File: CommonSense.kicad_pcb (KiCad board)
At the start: 2 copper layers, 35 x 24 mm, 36 parts, among them J1 Conn_02x04_Counter_Clockwise, J2 Conn_01x02, J3 Conn_01x02, J5 Conn_ARM_SWD_TagConnect_TC203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, U1 NRF52810-QFAA-R7, U2 SHT41-AD1B-R2, Y1 ECS-.327-12.5-12R-TR, Y2 ABM11W-32.0000MHZ-7-D1X-T3

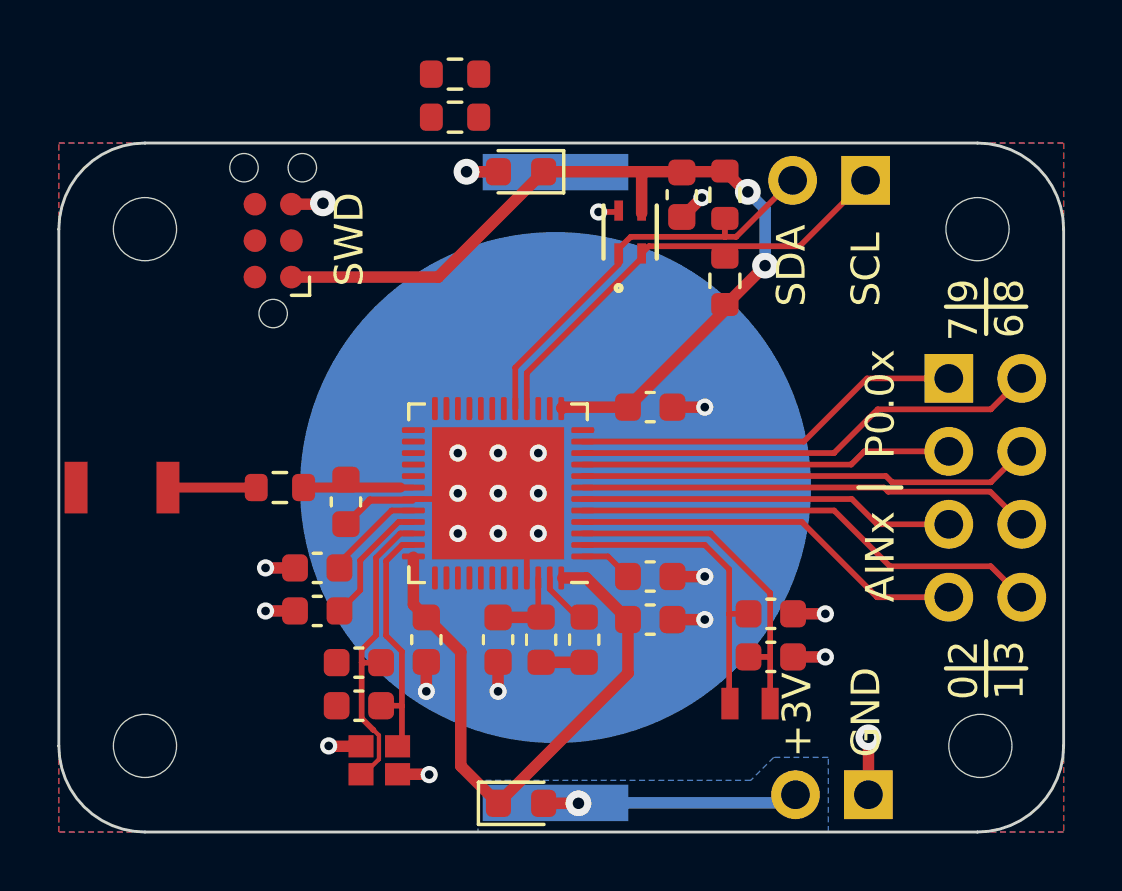
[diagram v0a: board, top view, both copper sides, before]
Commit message: Re-route SWD connector
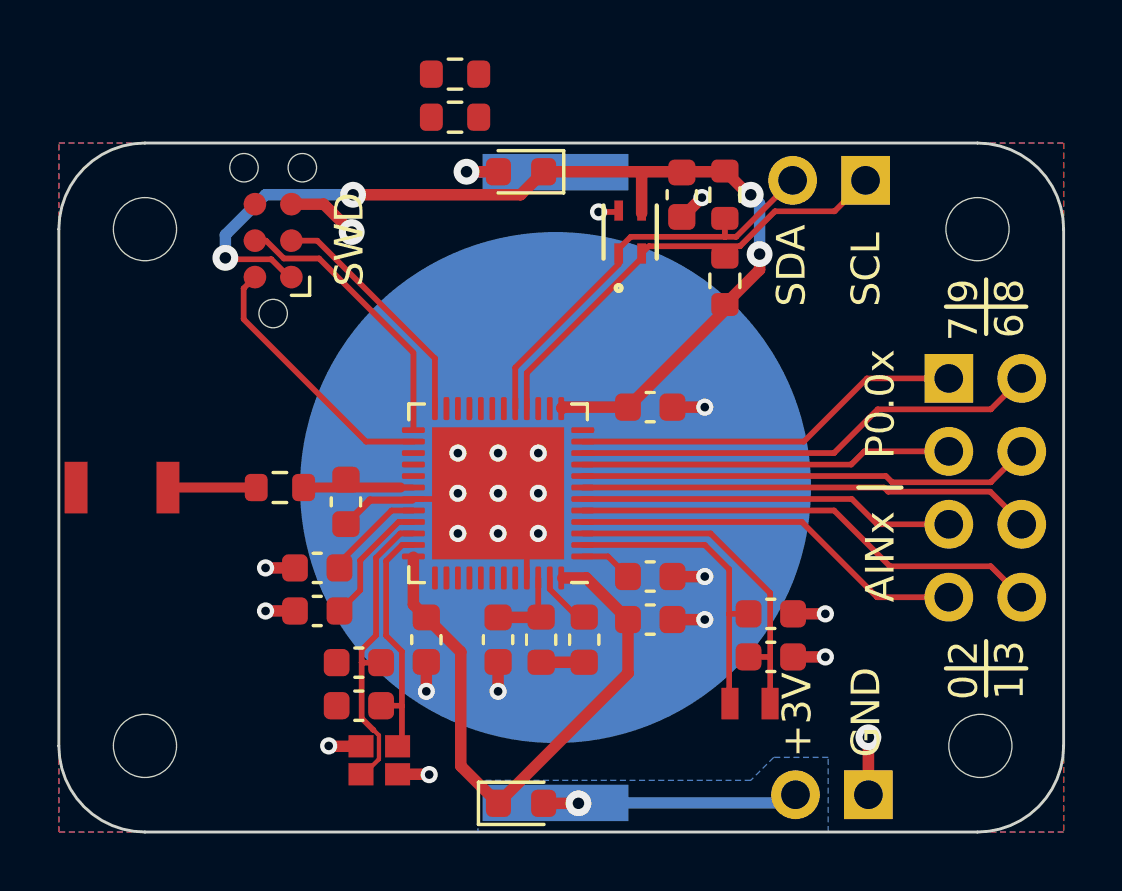
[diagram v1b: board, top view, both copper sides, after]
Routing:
- net /SWDCLK: track 0.00 -> 9.83 mm
- net /SWDIO: track 0.00 -> 9.31 mm
- net /NRESET: track 0.00 -> 8.45 mm
- net +3V0: track 52.2 -> 57.1 mm, vias 2 -> 4
- net GND: track 24.4 -> 25.8 mm
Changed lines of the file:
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@@
   )
   (segment (start 142.875 68) (end 139.8 68) (width 0.35) (layer "F.Cu") (net 1))
+  (segment (start 145.23 58.13) (end 144.1 58.13) (width 0.4) (layer "F.Cu") (net 2))
+  (segment (start 146.2 59.1) (end 145.23 58.13) (width 0.4) (layer "F.Cu") (net 2))
   (segment (start 148.887 77.987) (end 148.9 78) (width 0.4) (layer "F.Cu") (net 2))
   (segment (start 149.7 68.4) (end 149.9 68.2) (width 0.2) (layer "F.Cu") (net 2))
@@
   (segment (start 157.725 58.575) (end 158.4 57.9) (width 0.4) (layer "F.Cu") (net 2))
   (segment (start 145.413 77.013) (end 145.4 77) (width 0.4) (layer "F.Cu") (net 2))
-  (segment (start 144.1 58.13) (end 145.17 58.13) (width 0.4) (layer "F.Cu") (net 2))
   (segment (start 143.2 70.8) (end 144.225 70.8) (width 0.4) (layer "F.Cu") (net 2))
   (segment (start 157.7 58.575) (end 157.725 58.575) (width 0.4) (layer "F.Cu") (net 2))
@@
   (segment (start 161.575 72.4) (end 162.7 72.4) (width 0.4) (layer "F.Cu") (net 2))
   (segment (start 151.3 74.075) (end 151.3 75.1) (width 0.4) (layer "F.Cu") (net 2))
-  (segment (start 145.17 58.13) (end 145.2 58.1) (width 0.4) (layer "F.Cu") (net 2))
   (segment (start 154.8 58.4) (end 155.45305 58.4) (width 0.2) (layer "F.Cu") (net 2))
   (segment (start 146.5255 77.013) (end 145.413 77.013) (width 0.4) (layer "F.Cu") (net 2))
@@
   (via (at 151.3 69.6) (size 0.6) (drill 0.3) (layers "F.Cu" "B.Cu") (net 2))
   (via (at 158.5 71.1) (size 0.6) (drill 0.3) (layers "F.Cu" "B.Cu") (net 2))
-  (via (at 145.2 58.1) (size 0.9) (drill 0.4) (layers "F.Cu" "B.Cu") (net 2))
+  (via (at 146.2 59.1) (size 0.9) (drill 0.4) (layers "F.Cu" "B.Cu") (net 2))
   (via (at 148.9 78) (size 0.6) (drill 0.3) (layers "F.Cu" "B.Cu") (net 2))
   (via (at 149.9 68.2) (size 0.6) (drill 0.3) (layers "F.Cu" "B.Cu") (net 2))
@@
   (segment (start 154.25 69.2) (end 161.881891 69.2) (width 0.2) (layer "F.Cu") (net 21))
   (segment (start 161.881891 69.2) (end 164.501891 71.82) (width 0.2) (layer "F.Cu") (net 21))
+  (segment (start 143.8357 60.0207) (end 145.065991 60.0207) (width 0.2) (layer "F.Cu") (net 32))
+  (segment (start 143.215 59.4) (end 143.8357 60.0207) (width 0.2) (layer "F.Cu") (net 32))
+  (segment (start 148.35 63.304709) (end 148.35 66) (width 0.2) (layer "F.Cu") (net 32))
+  (segment (start 142.83 59.4) (end 143.215 59.4) (width 0.2) (layer "F.Cu") (net 32))
+  (segment (start 145.065991 60.0207) (end 148.35 63.304709) (width 0.2) (layer "F.Cu") (net 32))
+  (segment (start 142.83 60.67) (end 142.436301 61.063699) (width 0.2) (layer "F.Cu") (net 33))
+  (segment (start 142.436301 61.063699) (end 142.436301 62.136301) (width 0.2) (layer "F.Cu") (net 33))
+  (segment (start 142.436301 62.136301) (end 146.7 66.4) (width 0.2) (layer "F.Cu") (net 33))
+  (segment (start 146.7 66.4) (end 148.35 66.4) (width 0.2) (layer "F.Cu") (net 33))
   (segment (start 151.9 65.25) (end 151.9 63.822201) (width 0.2) (layer "F.Cu") (net 43))
   (segment (start 155.92025 59.266701) (end 159.2 59.266701) (width 0.2) (layer "F.Cu") (net 43))
@@
   (segment (start 151.9 63.822201) (end 155.49995 60.222251) (width 0.2) (layer "F.Cu") (net 43))
   (segment (start 155.49995 59.687001) (end 155.92025 59.266701) (width 0.2) (layer "F.Cu") (net 43))
-  (segment (start 156.553249 59.593701) (end 161.806299 59.593701) (width 0.2) (layer "F.Cu") (net 44))
+  (segment (start 160.945448 58.377) (end 163.023 58.377) (width 0.2) (layer "F.Cu") (net 44))
+  (segment (start 159.728747 59.593701) (end 160.945448 58.377) (width 0.2) (layer "F.Cu") (net 44))
   (segment (start 156.30005 60.006799) (end 156.30005 59.8469) (width 0.2) (layer "F.Cu") (net 44))
-  (segment (start 161.806299 59.593701) (end 164.1 57.3) (width 0.2) (layer "F.Cu") (net 44))
+  (segment (start 156.30005 59.8469) (end 156.553249 59.593701) (width 0.2) (layer "F.Cu") (net 44))
+  (segment (start 156.553249 59.593701) (end 159.728747 59.593701) (width 0.2) (layer "F.Cu") (net 44))
   (segment (start 152.3 64.006849) (end 156.30005 60.006799) (width 0.2) (layer "F.Cu") (net 44))
-  (segment (start 156.30005 59.8469) (end 156.553249 59.593701) (width 0.2) (layer "F.Cu") (net 44))
+  (segment (start 163.023 58.377) (end 164.1 57.3) (width 0.2) (layer "F.Cu") (net 44))
   (segment (start 152.3 65.25) (end 152.3 64.006849) (width 0.2) (layer "F.Cu") (net 44))
+  (segment (start 144.1 59.4) (end 145 59.4) (width 0.2) (layer "F.Cu") (net 46))
+  (segment (start 149.1 63.5) (end 149.1 65.25) (width 0.2) (layer "F.Cu") (net 46))
+  (segment (start 145 59.4) (end 149.1 63.5) (width 0.2) (layer "F.Cu") (net 46))
   (segment (start 153.1 71.541737) (end 154.070763 72.5125) (width 0.2) (layer "F.Cu") (net 47))
   (segment (start 154.070763 72.5125) (end 154.3 72.5125) (width 0.2) (layer "F.Cu") (net 47))
@@
   (segment (start 153.285 57) (end 153.3 57.015) (width 0.4) (layer "B.Cu") (net 49))
   (segment (start 153.3 78.985) (end 161.375 78.985) (width 0.4) (layer "B.Cu") (net 49))
+  (segment (start 143.401852 60.0493) (end 141.8493 60.0493) (width 0.2) (layer "F.Cu") (net 50))
   (segment (start 148.35 72.075) (end 148.35 70.427) (width 0.4) (layer "F.Cu") (net 50))
+  (segment (start 160.409948 60.415052) (end 159.2 61.625) (width 0.4) (layer "F.Cu") (net 50))
   (segment (start 156.3 57) (end 159.175 57) (width 0.4) (layer "F.Cu") (net 50))
   (segment (start 154.375 71.15) (end 153.552 71.15) (width 0.4) (layer "F.Cu") (net 50))
+  (segment (start 160.026642 57.801642) (end 159.2 56.975) (width 0.4) (layer "F.Cu") (net 50))
   (segment (start 156.3001 58.4531) (end 156.3001 57.0001) (width 0.4) (layer "F.Cu") (net 50))
   (segment (start 150 77.7) (end 150 73.725) (width 0.4) (layer "F.Cu") (net 50))
@@
   (segment (start 148.8 72.525) (end 148.35 72.075) (width 0.4) (layer "F.Cu") (net 50))
   (segment (start 155.825 74.475) (end 155.825 72.6) (width 0.4) (layer "F.Cu") (net 50))
-  (segment (start 144.1 60.67) (end 149.2175 60.67) (width 0.4) (layer "F.Cu") (net 50))
+  (segment (start 160.409948 59.869216) (end 160.409948 60.415052) (width 0.4) (layer "F.Cu") (net 50))
+  (segment (start 144.1 60.67) (end 144.022552 60.67) (width 0.2) (layer "F.Cu") (net 50))
   (segment (start 156.3001 57.0001) (end 156.3 57) (width 0.4) (layer "F.Cu") (net 50))
   (segment (start 152.8875 57) (end 156.3 57) (width 0.4) (layer "F.Cu") (net 50))
-  (segment (start 159.925 57.7) (end 159.2 56.975) (width 0.4) (layer "F.Cu") (net 50))
-  (segment (start 159.2 61.625) (end 159.245201 61.625) (width 0.4) (layer "F.Cu") (net 50))
+  (segment (start 160.101642 57.801642) (end 160.026642 57.801642) (width 0.4) (layer "F.Cu") (net 50))
   (segment (start 159.2 61.825) (end 155.825 65.2) (width 0.4) (layer "F.Cu") (net 50))
-  (segment (start 159.245201 61.625) (end 160.6 60.270201) (width 0.4) (layer "F.Cu") (net 50))
-  (segment (start 149.2175 60.67) (end 152.8875 57) (width 0.4) (layer "F.Cu") (net 50))
-  (segment (start 160 57.7) (end 159.925 57.7) (width 0.4) (layer "F.Cu") (net 50))
+  (segment (start 144.022552 60.67) (end 143.401852 60.0493) (width 0.2) (layer "F.Cu") (net 50))
+  (segment (start 146.247897 57.802) (end 152.0855 57.802) (width 0.4) (layer "F.Cu") (net 50))
+  (segment (start 152.0855 57.802) (end 152.8875 57) (width 0.4) (layer "F.Cu") (net 50))
   (segment (start 155.825 65.2) (end 153.55 65.2) (width 0.4) (layer "F.Cu") (net 50))
   (segment (start 159.175 57) (end 159.2 56.975) (width 0.4) (layer "F.Cu") (net 50))
   (segment (start 153.527 65.223) (end 153.527 65.25) (width 0.4) (layer "F.Cu") (net 50))
   (segment (start 150 73.725) (end 148.8 72.525) (width 0.4) (layer "F.Cu") (net 50))
+  (segment (start 141.8493 60.0493) (end 141.8 60) (width 0.2) (layer "F.Cu") (net 50))
   (segment (start 151.3 79) (end 150 77.7) (width 0.4) (layer "F.Cu") (net 50))
   (segment (start 155.825 72.6) (end 154.375 71.15) (width 0.4) (layer "F.Cu") (net 50))
   (segment (start 151.3 79) (end 155.825 74.475) (width 0.4) (layer "F.Cu") (net 50))
-  (via (at 160.6 60.270201) (size 0.9) (drill 0.4) (layers "F.Cu" "B.Cu") (net 50))
-  (via (at 160 57.7) (size 0.9) (drill 0.4) (layers "F.Cu" "B.Cu") (net 50))
-  (segment (start 160.6 60.270201) (end 160.6 58.3) (width 0.4) (layer "B.Cu") (net 50))
-  (segment (start 160.6 58.3) (end 160 57.7) (width 0.4) (layer "B.Cu") (net 50))
+  (via (at 160.409948 59.869216) (size 0.9) (drill 0.4) (layers "F.Cu" "B.Cu") (net 50))
+  (via (at 160.101642 57.801642) (size 0.9) (drill 0.4) (layers "F.Cu" "B.Cu") (net 50))
+  (via (at 141.8 60) (size 0.9) (drill 0.4) (layers "F.Cu" "B.Cu") (net 50))
+  (via (at 146.247897 57.802) (size 0.9) (drill 0.4) (layers "F.Cu" "B.Cu") (net 50))
+  (segment (start 160.409948 58.109948) (end 160.409948 59.869216) (width 0.4) (layer "B.Cu") (net 50))
+  (segment (start 144.089444 57.8053) (end 144.084144 57.8) (width 0.4) (layer "B.Cu") (net 50))
+  (segment (start 144.877856 57.8) (end 144.872556 57.8053) (width 0.4) (layer "B.Cu") (net 50))
+  (segment (start 146.247897 57.802) (end 146.245897 57.8) (width 0.4) (layer "B.Cu") (net 50))
+  (segment (start 144.084144 57.8) (end 143.2 57.8) (width 0.4) (layer "B.Cu") (net 50))
+  (segment (start 146.245897 57.8) (end 144.877856 57.8) (width 0.4) (layer "B.Cu") (net 50))
+  (segment (start 144.872556 57.8053) (end 144.089444 57.8053) (width 0.4) (layer "B.Cu") (net 50))
+  (segment (start 141.8 59.2) (end 141.8 60) (width 0.4) (layer "B.Cu") (net 50))
+  (segment (start 160.101642 57.801642) (end 160.409948 58.109948) (width 0.4) (layer "B.Cu") (net 50))
+  (segment (start 143.2 57.8) (end 141.8 59.2) (width 0.4) (layer "B.Cu") (net 50))
   (zone (net 0) (net_name "") (layer "F.Cu") (hatch edge 0.5)
     (connect_pads yes (clearance 0))
